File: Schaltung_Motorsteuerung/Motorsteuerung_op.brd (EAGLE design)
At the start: 100 x 64.8 mm, 22 parts, among them IC1 ULN2003AN, IC2 LM324P, X1 22-23-2021, X2 22-23-2021, X3 22-23-2021, X5 22-23-2021

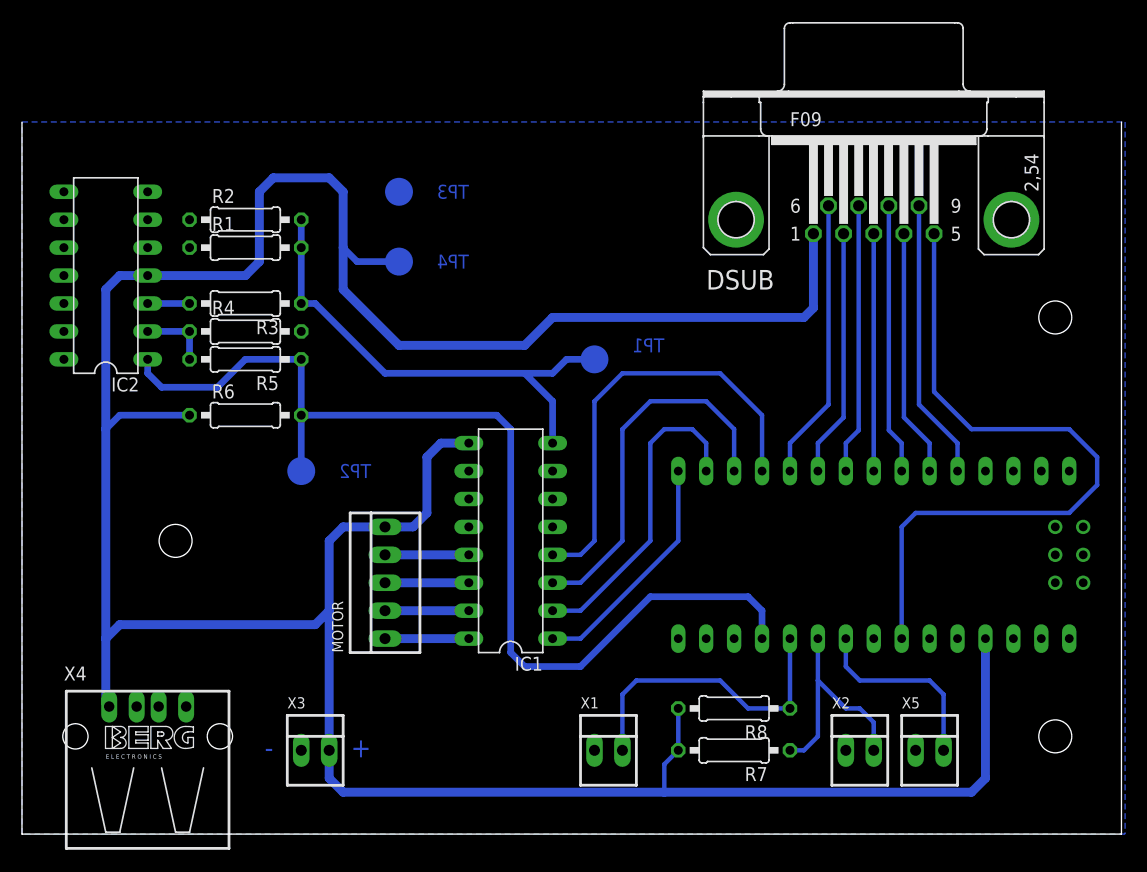
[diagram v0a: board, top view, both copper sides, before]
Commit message: Update 3
Added electric cirquit diagrams,
pin-routing-table,
description of  IR-Module
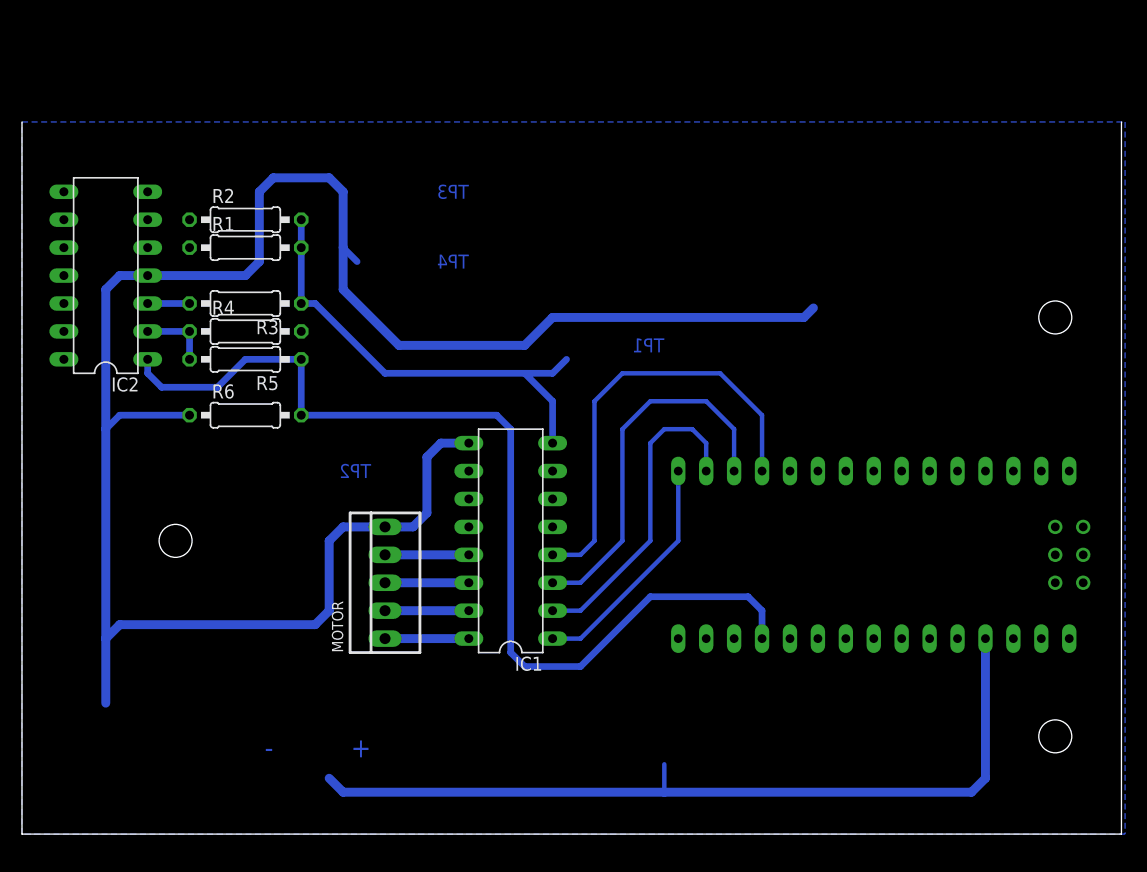
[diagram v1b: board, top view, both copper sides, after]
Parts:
- removed DSUB: (no value), con-subd:F09HP
- removed R7, R8: 4K7, rcl:0207/10
- removed TP1, TP2, TP3, TP4: TPB2,54, testpad:B2,54
- removed X1, X2, X3, X5: 22-23-2021, con-molex:22-23-2021
- removed X4: (no value), con-berg:PN87520
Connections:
- removed net N$10: DSUB.2, U$1.D7
- removed net N$11: DSUB.7, U$1.D6
- removed net N$12: DSUB.3, U$1.D5
- removed net N$13: DSUB.8, U$1.D4
- removed net N$14: DSUB.4, U$1.D3
- removed net N$15: DSUB.9, U$1.D2
- removed net N$16: DSUB.6, U$1.D8
- removed net N$20: DSUB.5, U$1.A5
- removed net N$21: R8.1, U$1.A1, X1.2
- removed net N$22: R7.1, U$1.A2, X2.2
- removed net N$24: U$1.A3, X5.2
- net GND: no longer DSUB.G1, TP3.TP, U$1.GND1, X1.1, X2.1, X3.1, X4.4, X5.1
- net N$18: no longer TP2.TP
- net N$9: no longer TP1.TP
- net VCC: no longer DSUB.1, R7.2, R8.2, TP4.TP, X3.2, X4.1
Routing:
- net N$20: track 63.7 -> 0.00 mm
- net VCC: track 287.7 -> 255.8 mm
- net N$21: track 28.2 -> 0.00 mm
- net N$16: track 25.6 -> 0.00 mm
- net N$15: track 25.6 -> 0.00 mm
- net N$13: track 24.6 -> 0.00 mm
- net N$11: track 24.6 -> 0.00 mm
- net N$14: track 22.6 -> 0.00 mm
- net N$10: track 22.6 -> 0.00 mm
- net N$12: track 21.6 -> 0.00 mm
- net N$22: track 21.2 -> 0.00 mm
- net N$24: track 17.6 -> 0.00 mm
- net N$18: track 96.0 -> 90.9 mm
- net N$9: track 44.8 -> 42.3 mm
